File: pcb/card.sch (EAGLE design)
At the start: 18 parts, among them IC1 74HC14D, IC2 W25X32, Q1 BC817

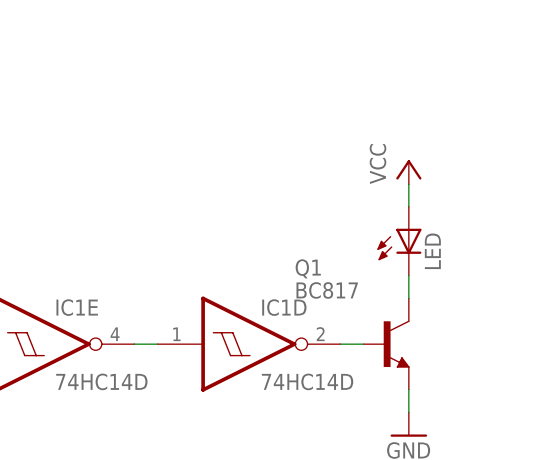
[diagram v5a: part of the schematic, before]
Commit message: Added a current limitting resistor to the LED.
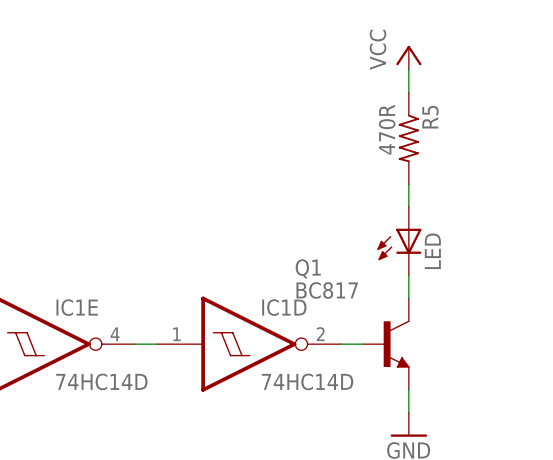
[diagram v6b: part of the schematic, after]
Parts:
- added R5: 470R, resistor:R-US_M1206
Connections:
- new net N$3: LED.A, R5.2
- net VCC: now also R5.1; no longer LED.A
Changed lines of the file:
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@@
 <part name="GND" library="testpad" deviceset="TP" device="B1,27"/>
 <part name="D1" library="diode" deviceset="DIODE-" device="MINIMELF"/>
+<part name="R5" library="resistor" deviceset="R-US_" device="M1206" value="470R"/>
 </parts>
 <sheets>
@@
 <instance part="P+1" gate="VCC" x="60.96" y="22.86"/>
 <instance part="P+2" gate="VCC" x="30.48" y="68.58"/>
-<instance part="P+3" gate="VCC" x="137.16" y="71.12"/>
+<instance part="P+3" gate="VCC" x="137.16" y="83.82"/>
 <instance part="R1" gate="G$1" x="-5.08" y="58.42" rot="R90"/>
 <instance part="R3" gate="G$1" x="60.96" y="50.8" rot="R180"/>
@@
 </instance>
 <instance part="D1" gate="G$1" x="-5.08" y="45.72" rot="R90"/>
+<instance part="R5" gate="G$1" x="137.16" y="73.66" rot="R270"/>
 </instances>
 <busses>
@@
 </segment>
 <segment>
-<pinref part="LED" gate="G$1" pin="A"/>
-<pinref part="P+3" gate="VCC" pin="VCC"/>
-<wire x1="137.16" y1="66.04" x2="137.16" y2="68.58" width="0.1524" layer="91"/>
-</segment>
-<segment>
 <pinref part="P+1" gate="VCC" pin="VCC"/>
 <pinref part="C3" gate="G$1" pin="2"/>
@@
 <pinref part="IC2" gate="G$1" pin="!HOLD!"/>
 <wire x1="101.6" y1="15.24" x2="106.68" y2="15.24" width="0.1524" layer="91"/>
+</segment>
+<segment>
+<pinref part="R5" gate="G$1" pin="1"/>
+<pinref part="P+3" gate="VCC" pin="VCC"/>
+<wire x1="137.16" y1="81.28" x2="137.16" y2="78.74" width="0.1524" layer="91"/>
 </segment>
 </net>
@@
 </segment>
 </net>
-<net name="N$13" class="0">
-<segment>
-<pinref part="Q1" gate="G$1" pin="C"/>
-<pinref part="LED" gate="G$1" pin="C"/>
-<wire x1="137.16" y1="55.88" x2="137.16" y2="58.42" width="0.1524" layer="91"/>
-</segment>
-</net>
 <net name="N$10" class="0">
 <segment>
@@
 </segment>
 </net>
+<net name="N$3" class="0">
+<segment>
+<pinref part="LED" gate="G$1" pin="A"/>
+<pinref part="R5" gate="G$1" pin="2"/>
+<wire x1="137.16" y1="68.58" x2="137.16" y2="66.04" width="0.1524" layer="91"/>
+</segment>
+</net>
+<net name="N$4" class="0">
+<segment>
+<pinref part="Q1" gate="G$1" pin="C"/>
+<pinref part="LED" gate="G$1" pin="C"/>
+<wire x1="137.16" y1="58.42" x2="137.16" y2="55.88" width="0.1524" layer="91"/>
+</segment>
+</net>

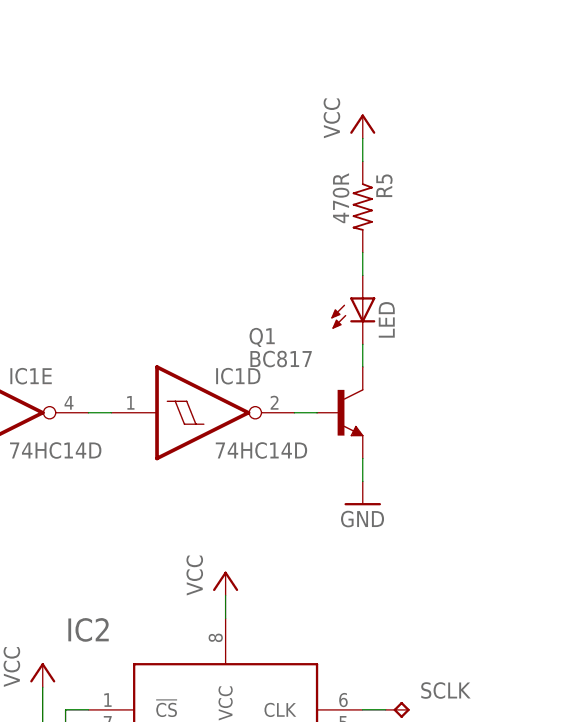
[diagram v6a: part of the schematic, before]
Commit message: Swapped the NPN tranny for a MOSFET.
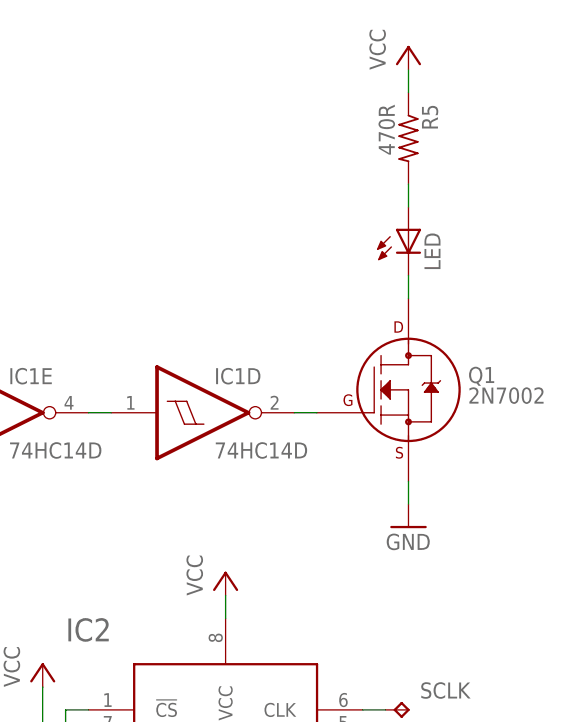
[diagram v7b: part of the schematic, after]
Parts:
- Q1: value BC817 -> 2N7002; device transistor:BC817-16-NPN-SOT23-BEC -> transistors:2N7000_SOT23
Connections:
- net GND: now also Q1.S; no longer Q1.E
- net N$12: now also Q1.G; no longer Q1.B
- net N$4: now also Q1.D; no longer Q1.C
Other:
- moved on the sheet: LED, R5
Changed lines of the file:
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@@
 <part name="IC1" library="74xx-eu" deviceset="74*14" device="D" technology="HC"/>
 <part name="D2" library="diode" deviceset="DIODE-" device="MINIMELF"/>
-<part name="Q1" library="transistor" deviceset="*-NPN-" device="SOT23-BEC" technology="BC817-16" value="BC817"/>
 <part name="LED" library="led" deviceset="LED" device="CHIPLED_1206"/>
 <part name="R2" library="resistor" deviceset="R-US_" device="M1206" value="470k"/>
@@
 <part name="D1" library="diode" deviceset="DIODE-" device="MINIMELF"/>
 <part name="R5" library="resistor" deviceset="R-US_" device="M1206" value="470R"/>
+<part name="Q1" library="transistors" deviceset="2N700*" device="_SOT23" technology="0" value="2N7002"/>
 </parts>
 <sheets>
@@
 <instance part="P+1" gate="VCC" x="60.96" y="22.86"/>
 <instance part="P+2" gate="VCC" x="30.48" y="68.58"/>
-<instance part="P+3" gate="VCC" x="137.16" y="83.82"/>
+<instance part="P+3" gate="VCC" x="142.24" y="91.44"/>
 <instance part="R1" gate="G$1" x="-5.08" y="58.42" rot="R90"/>
 <instance part="R3" gate="G$1" x="60.96" y="50.8" rot="R180"/>
@@
 <instance part="GND3" gate="1" x="-7.62" y="0"/>
 <instance part="GND4" gate="1" x="81.28" y="25.4"/>
-<instance part="GND5" gate="1" x="137.16" y="40.64"/>
+<instance part="GND5" gate="1" x="142.24" y="38.1"/>
 <instance part="IC1" gate="A" x="17.78" y="50.8"/>
 <instance part="IC1" gate="B" x="5.08" y="22.86"/>
@@
 <instance part="IC1" gate="F" x="43.18" y="50.8"/>
 <instance part="D2" gate="G$1" x="73.66" y="50.8"/>
-<instance part="Q1" gate="G$1" x="134.62" y="50.8"/>
-<instance part="LED" gate="G$1" x="137.16" y="63.5"/>
+<instance part="LED" gate="G$1" x="142.24" y="71.12"/>
 <instance part="R2" gate="G$1" x="30.48" y="58.42" rot="R90"/>
 <instance part="C3" gate="G$1" x="60.96" y="10.16" rot="R180"/>
@@
 </instance>
 <instance part="D1" gate="G$1" x="-5.08" y="45.72" rot="R90"/>
-<instance part="R5" gate="G$1" x="137.16" y="73.66" rot="R270"/>
+<instance part="R5" gate="G$1" x="142.24" y="81.28" rot="R270"/>
+<instance part="Q1" gate="G$1" x="142.24" y="53.34"/>
 </instances>
 <busses>
@@
 </segment>
 <segment>
-<pinref part="Q1" gate="G$1" pin="E"/>
 <pinref part="GND5" gate="1" pin="GND"/>
-<wire x1="137.16" y1="45.72" x2="137.16" y2="43.18" width="0.1524" layer="91"/>
+<wire x1="142.24" y1="43.18" x2="142.24" y2="40.64" width="0.1524" layer="91"/>
+<pinref part="Q1" gate="G$1" pin="S"/>
 </segment>
 <segment>
@@
 <pinref part="R5" gate="G$1" pin="1"/>
 <pinref part="P+3" gate="VCC" pin="VCC"/>
-<wire x1="137.16" y1="81.28" x2="137.16" y2="78.74" width="0.1524" layer="91"/>
+<wire x1="142.24" y1="88.9" x2="142.24" y2="86.36" width="0.1524" layer="91"/>
 </segment>
 </net>
@@
 <segment>
 <pinref part="IC1" gate="D" pin="O"/>
-<pinref part="Q1" gate="G$1" pin="B"/>
 <wire x1="129.54" y1="50.8" x2="132.08" y2="50.8" width="0.1524" layer="91"/>
+<pinref part="Q1" gate="G$1" pin="G"/>
 </segment>
 </net>
@@
 <pinref part="LED" gate="G$1" pin="A"/>
 <pinref part="R5" gate="G$1" pin="2"/>
-<wire x1="137.16" y1="68.58" x2="137.16" y2="66.04" width="0.1524" layer="91"/>
+<wire x1="142.24" y1="76.2" x2="142.24" y2="73.66" width="0.1524" layer="91"/>
 </segment>
 </net>
 <net name="N$4" class="0">
 <segment>
-<pinref part="Q1" gate="G$1" pin="C"/>
 <pinref part="LED" gate="G$1" pin="C"/>
-<wire x1="137.16" y1="58.42" x2="137.16" y2="55.88" width="0.1524" layer="91"/>
-</segment>
-</net>
+<wire x1="142.24" y1="66.04" x2="142.24" y2="63.5" width="0.1524" layer="91"/>
+<pinref part="Q1" gate="G$1" pin="D"/>
+</segment>
+</net>

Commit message: Compacted & improved the design.
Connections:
- net GND: now also IC1D.I, IC1E.I; no longer IC1B.I, IC1C.I
- net N$11: now also IC1C.O, IC1F.I; no longer IC1D.I, IC1E.O
- net N$12: now also IC1F.O; no longer IC1D.O
- net N$5: now also IC1B.I; no longer IC1F.I
- net N$6: now also IC1B.O; no longer IC1F.O
- net N$8: now also IC1C.I; no longer IC1E.I
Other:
- moved on the sheet: IC1B, IC1C, IC1D, IC1E, IC1F, LED, Q1, R5
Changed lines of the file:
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@@
 <instance part="P+1" gate="VCC" x="60.96" y="22.86"/>
 <instance part="P+2" gate="VCC" x="30.48" y="68.58"/>
-<instance part="P+3" gate="VCC" x="142.24" y="91.44"/>
+<instance part="P+3" gate="VCC" x="139.7" y="91.44"/>
 <instance part="R1" gate="G$1" x="-5.08" y="58.42" rot="R90"/>
 <instance part="R3" gate="G$1" x="60.96" y="50.8" rot="R180"/>
@@
 <instance part="GND3" gate="1" x="-7.62" y="0"/>
 <instance part="GND4" gate="1" x="81.28" y="25.4"/>
-<instance part="GND5" gate="1" x="142.24" y="38.1"/>
+<instance part="GND5" gate="1" x="139.7" y="38.1"/>
 <instance part="IC1" gate="A" x="17.78" y="50.8"/>
-<instance part="IC1" gate="B" x="5.08" y="22.86"/>
-<instance part="IC1" gate="C" x="5.08" y="7.62"/>
-<instance part="IC1" gate="D" x="119.38" y="50.8"/>
-<instance part="IC1" gate="E" x="96.52" y="50.8"/>
-<instance part="IC1" gate="F" x="43.18" y="50.8"/>
+<instance part="IC1" gate="B" x="43.18" y="50.8"/>
+<instance part="IC1" gate="C" x="93.98" y="50.8"/>
+<instance part="IC1" gate="D" x="5.08" y="22.86"/>
+<instance part="IC1" gate="E" x="5.08" y="10.16"/>
+<instance part="IC1" gate="F" x="116.84" y="50.8"/>
 <instance part="D2" gate="G$1" x="73.66" y="50.8"/>
-<instance part="LED" gate="G$1" x="142.24" y="71.12"/>
+<instance part="LED" gate="G$1" x="139.7" y="71.12"/>
 <instance part="R2" gate="G$1" x="30.48" y="58.42" rot="R90"/>
 <instance part="C3" gate="G$1" x="60.96" y="10.16" rot="R180"/>
@@
 </instance>
 <instance part="D1" gate="G$1" x="-5.08" y="45.72" rot="R90"/>
-<instance part="R5" gate="G$1" x="142.24" y="81.28" rot="R270"/>
-<instance part="Q1" gate="G$1" x="142.24" y="53.34"/>
+<instance part="R5" gate="G$1" x="139.7" y="81.28" rot="R270"/>
+<instance part="Q1" gate="G$1" x="139.7" y="53.34"/>
 </instances>
 <busses>
@@
 <net name="GND" class="0">
 <segment>
-<pinref part="IC1" gate="B" pin="I"/>
 <pinref part="GND3" gate="1" pin="GND"/>
-<wire x1="-5.08" y1="22.86" x2="-7.62" y2="22.86" width="0.1524" layer="91"/>
-<wire x1="-7.62" y1="22.86" x2="-7.62" y2="7.62" width="0.1524" layer="91"/>
-<pinref part="IC1" gate="C" pin="I"/>
-<wire x1="-7.62" y1="7.62" x2="-7.62" y2="2.54" width="0.1524" layer="91"/>
-<wire x1="-5.08" y1="7.62" x2="-7.62" y2="7.62" width="0.1524" layer="91"/>
-<junction x="-7.62" y="7.62"/>
+<wire x1="-7.62" y1="22.86" x2="-7.62" y2="10.16" width="0.1524" layer="91"/>
+<wire x1="-7.62" y1="10.16" x2="-7.62" y2="2.54" width="0.1524" layer="91"/>
+<pinref part="IC1" gate="E" pin="I"/>
+<wire x1="-5.08" y1="10.16" x2="-7.62" y2="10.16" width="0.1524" layer="91"/>
+<junction x="-7.62" y="10.16"/>
+<pinref part="IC1" gate="D" pin="I"/>
+<wire x1="-7.62" y1="22.86" x2="-5.08" y2="22.86" width="0.1524" layer="91"/>
 </segment>
 <segment>
@@
 <segment>
 <pinref part="GND5" gate="1" pin="GND"/>
-<wire x1="142.24" y1="43.18" x2="142.24" y2="40.64" width="0.1524" layer="91"/>
+<wire x1="139.7" y1="43.18" x2="139.7" y2="40.64" width="0.1524" layer="91"/>
 <pinref part="Q1" gate="G$1" pin="S"/>
 </segment>
@@
 <net name="N$5" class="0">
 <segment>
-<pinref part="IC1" gate="F" pin="I"/>
 <pinref part="R2" gate="G$1" pin="1"/>
-<wire x1="30.48" y1="50.8" x2="33.02" y2="50.8" width="0.1524" layer="91"/>
 <wire x1="30.48" y1="53.34" x2="30.48" y2="50.8" width="0.1524" layer="91"/>
 <pinref part="IC1" gate="A" pin="O"/>
 <wire x1="30.48" y1="50.8" x2="27.94" y2="50.8" width="0.1524" layer="91"/>
+<pinref part="IC1" gate="B" pin="I"/>
+<wire x1="33.02" y1="50.8" x2="30.48" y2="50.8" width="0.1524" layer="91"/>
 <junction x="30.48" y="50.8"/>
 </segment>
@@
 <pinref part="R5" gate="G$1" pin="1"/>
 <pinref part="P+3" gate="VCC" pin="VCC"/>
-<wire x1="142.24" y1="88.9" x2="142.24" y2="86.36" width="0.1524" layer="91"/>
-</segment>
-</net>
-<net name="N$6" class="0">
-<segment>
-<pinref part="IC1" gate="F" pin="O"/>
-<pinref part="R3" gate="G$1" pin="2"/>
-<wire x1="53.34" y1="50.8" x2="55.88" y2="50.8" width="0.1524" layer="91"/>
+<wire x1="139.7" y1="88.9" x2="139.7" y2="86.36" width="0.1524" layer="91"/>
 </segment>
 </net>
@@
 <segment>
 <pinref part="D2" gate="G$1" pin="C"/>
-<pinref part="IC1" gate="E" pin="I"/>
 <wire x1="76.2" y1="50.8" x2="81.28" y2="50.8" width="0.1524" layer="91"/>
-<wire x1="86.36" y1="50.8" x2="81.28" y2="50.8" width="0.1524" layer="91"/>
 <wire x1="81.28" y1="50.8" x2="81.28" y2="45.72" width="0.1524" layer="91"/>
 <pinref part="R4" gate="G$1" pin="1"/>
@@
 <wire x1="83.82" y1="45.72" x2="83.82" y2="40.64" width="0.1524" layer="91"/>
 <junction x="81.28" y="45.72"/>
+<pinref part="IC1" gate="C" pin="I"/>
+<wire x1="83.82" y1="50.8" x2="81.28" y2="50.8" width="0.1524" layer="91"/>
 <junction x="81.28" y="50.8"/>
-</segment>
-</net>
-<net name="N$11" class="0">
-<segment>
-<pinref part="IC1" gate="E" pin="O"/>
-<pinref part="IC1" gate="D" pin="I"/>
-<wire x1="106.68" y1="50.8" x2="109.22" y2="50.8" width="0.1524" layer="91"/>
-</segment>
-</net>
-<net name="N$12" class="0">
-<segment>
-<pinref part="IC1" gate="D" pin="O"/>
-<wire x1="129.54" y1="50.8" x2="132.08" y2="50.8" width="0.1524" layer="91"/>
-<pinref part="Q1" gate="G$1" pin="G"/>
 </segment>
 </net>
@@
 <pinref part="LED" gate="G$1" pin="A"/>
 <pinref part="R5" gate="G$1" pin="2"/>
-<wire x1="142.24" y1="76.2" x2="142.24" y2="73.66" width="0.1524" layer="91"/>
+<wire x1="139.7" y1="76.2" x2="139.7" y2="73.66" width="0.1524" layer="91"/>
 </segment>
 </net>
@@
 <segment>
 <pinref part="LED" gate="G$1" pin="C"/>
-<wire x1="142.24" y1="66.04" x2="142.24" y2="63.5" width="0.1524" layer="91"/>
+<wire x1="139.7" y1="66.04" x2="139.7" y2="63.5" width="0.1524" layer="91"/>
 <pinref part="Q1" gate="G$1" pin="D"/>
 </segment>
 </net>
+<net name="N$12" class="0">
+<segment>
+<pinref part="Q1" gate="G$1" pin="G"/>
+<pinref part="IC1" gate="F" pin="O"/>
+<wire x1="127" y1="50.8" x2="129.54" y2="50.8" width="0.1524" layer="91"/>
+</segment>
+</net>
+<net name="N$6" class="0">
+<segment>
+<pinref part="R3" gate="G$1" pin="2"/>
+<pinref part="IC1" gate="B" pin="O"/>
+<wire x1="53.34" y1="50.8" x2="55.88" y2="50.8" width="0.1524" layer="91"/>
+</segment>
+</net>
+<net name="N$11" class="0">
+<segment>
+<pinref part="IC1" gate="F" pin="I"/>
+<pinref part="IC1" gate="C" pin="O"/>
+<wire x1="104.14" y1="50.8" x2="106.68" y2="50.8" width="0.1524" layer="91"/>
+</segment>
+</net>
